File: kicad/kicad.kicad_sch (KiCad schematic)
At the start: 231 parts, among them sw1 Esc, sw10 Z, sw100 Num5, sw101 Num6, sw102 Num2, sw103 Num1, sw104 Num0, sw105 mPlay, sw106 mFwd, sw107 Num/, sw108 Num*, sw109 Num8, sw11 LCtrl, sw110 Num9, sw111 Num-, sw112 Num+, sw113 NumEnter, sw114 Num3, sw115 Num., sw12 LSys, sw13 F2, sw14 F3, sw15 2, sw16 3, sw17 W, sw18 E, sw19 S, sw2 F1, sw20 D, sw21 X, sw22 C, sw23 LAlt, sw24 THome, sw25 F4, sw26 F5, sw27 4, sw28 5, sw29 R, sw3 Tilda, sw30 T, sw31 F, sw32 G, sw33 V, sw34 B, sw35 LSpace, sw36 TLeft, sw37 F6, sw38 F7, sw39 6, sw4 1, sw40 7, sw41 Y, sw42 U, sw43 H, sw44 J, sw45 N, sw46 M, sw47 TUp, sw48 TDown, sw49 F8, sw5 Tab, sw50 F9, sw51 8, sw52 9, sw53 I, sw54 O, sw55 K, sw56 L, sw57 ,, sw58 ., sw59 RSpace, sw6 Q, sw60 TRight, sw61 F10, sw62 F11, sw63 0, sw64 -, sw65 P, sw66 [, sw67 ;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

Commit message: startup pcb
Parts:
- sw100: value Num5 -> N5
- sw101: value Num6 -> N6
- sw102: value Num2 -> N2
- sw103: value Num1 -> N1
- sw104: value Num0 -> N0
- sw105: value mPlay -> MPlay
- sw106: value mFwd -> MFwd
- sw107: value Num/ -> NSlash
- sw108: value Num* -> NStar
- sw109: value Num8 -> N8
- sw110: value Num9 -> N9
- sw111: value Num- -> NMinus
- sw112: value Num+ -> NPlus
- sw113: value NumEnter -> NEnter
- sw114: value Num3 -> N3
- sw115: value Num. -> NPeriod
- sw57: value , -> Comma
- sw58: value . -> Period
- sw64: value - -> Minus
- sw66: value [ -> LBrack
- sw67: value ; -> Semi
- sw68: value ' -> Quote
- sw69: value / -> FSlash
- sw75: value = -> Equals
- sw77: value ] -> RBrack
- sw78: value \ -> BSlash
- sw83: value ScrLck -> Scroll
- sw89: value Num4 -> N4
- sw94: value FN -> Fn
- sw95: value mBack -> MBack
- sw97: value NumLck -> NLock
- sw99: value Num7 -> N7

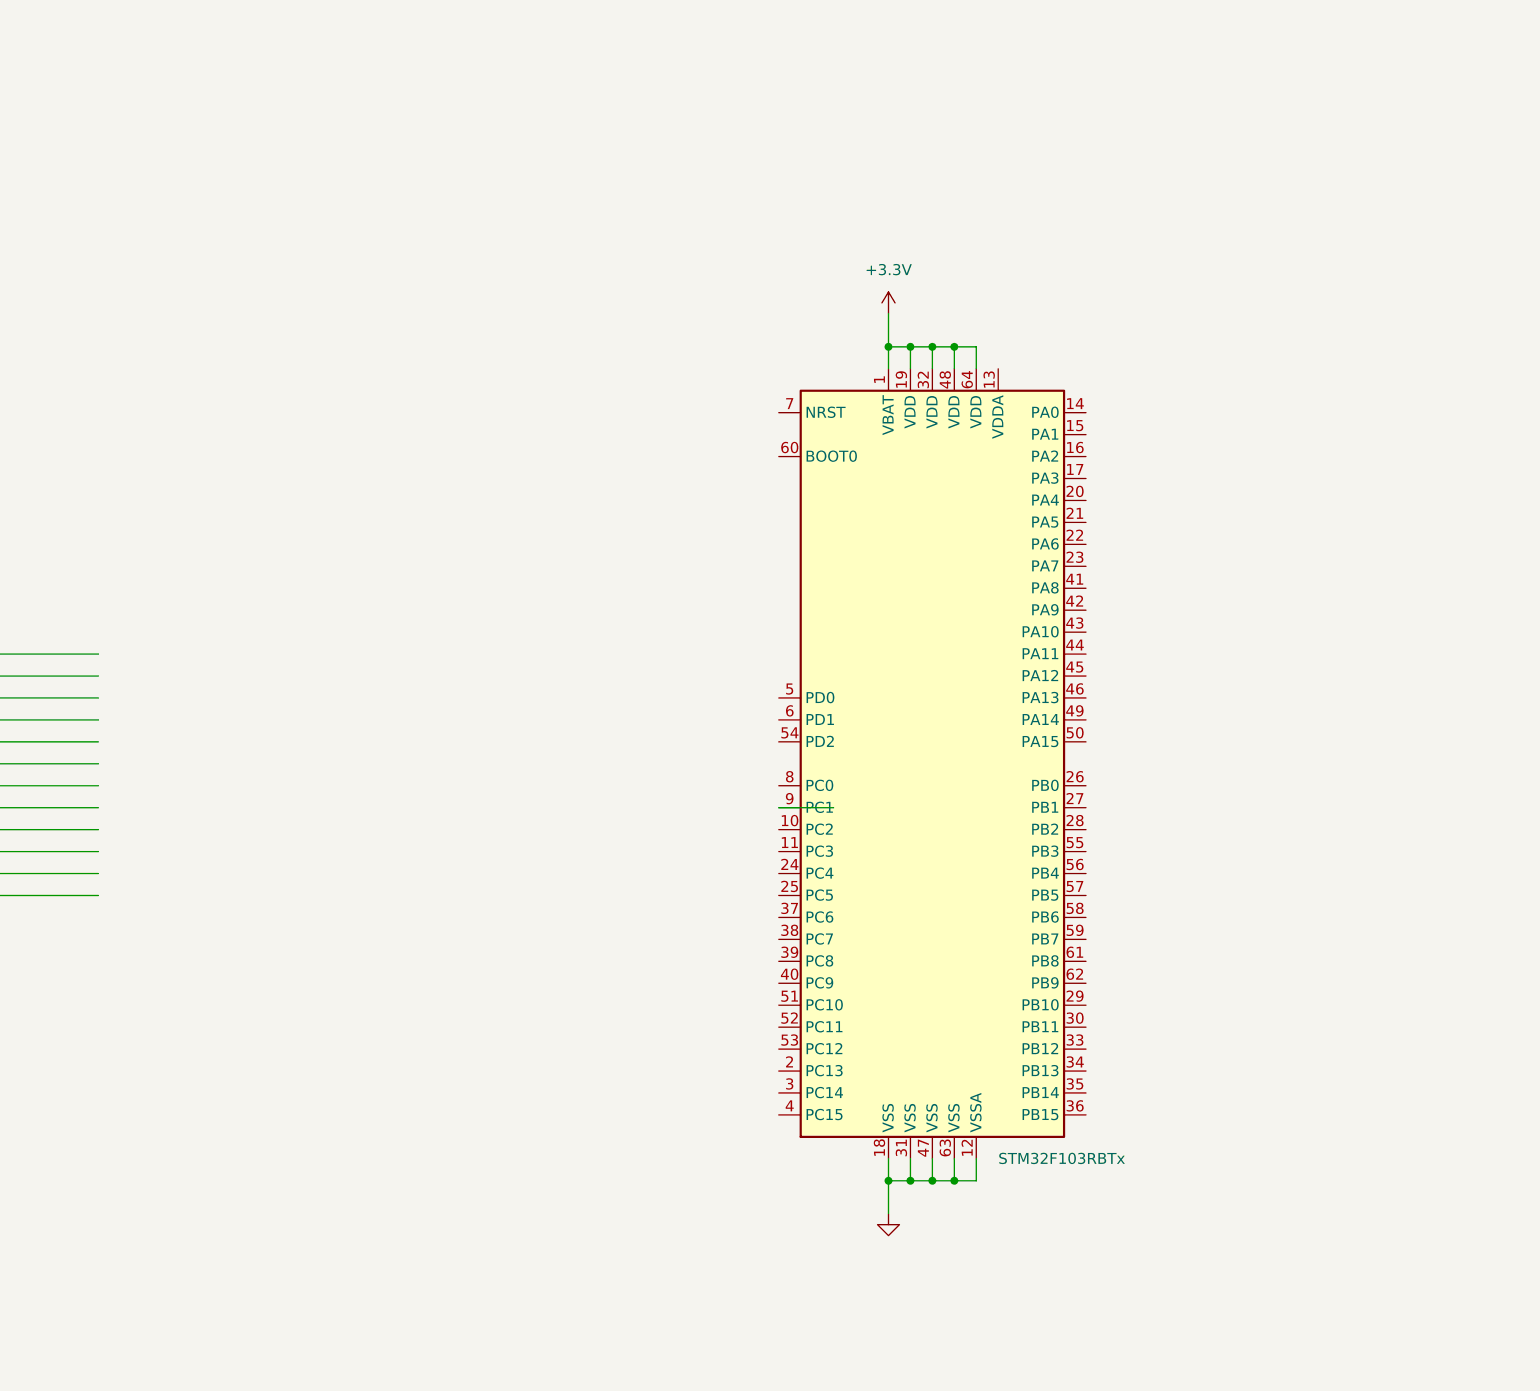
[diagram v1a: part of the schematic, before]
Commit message: Add decoupling circuits
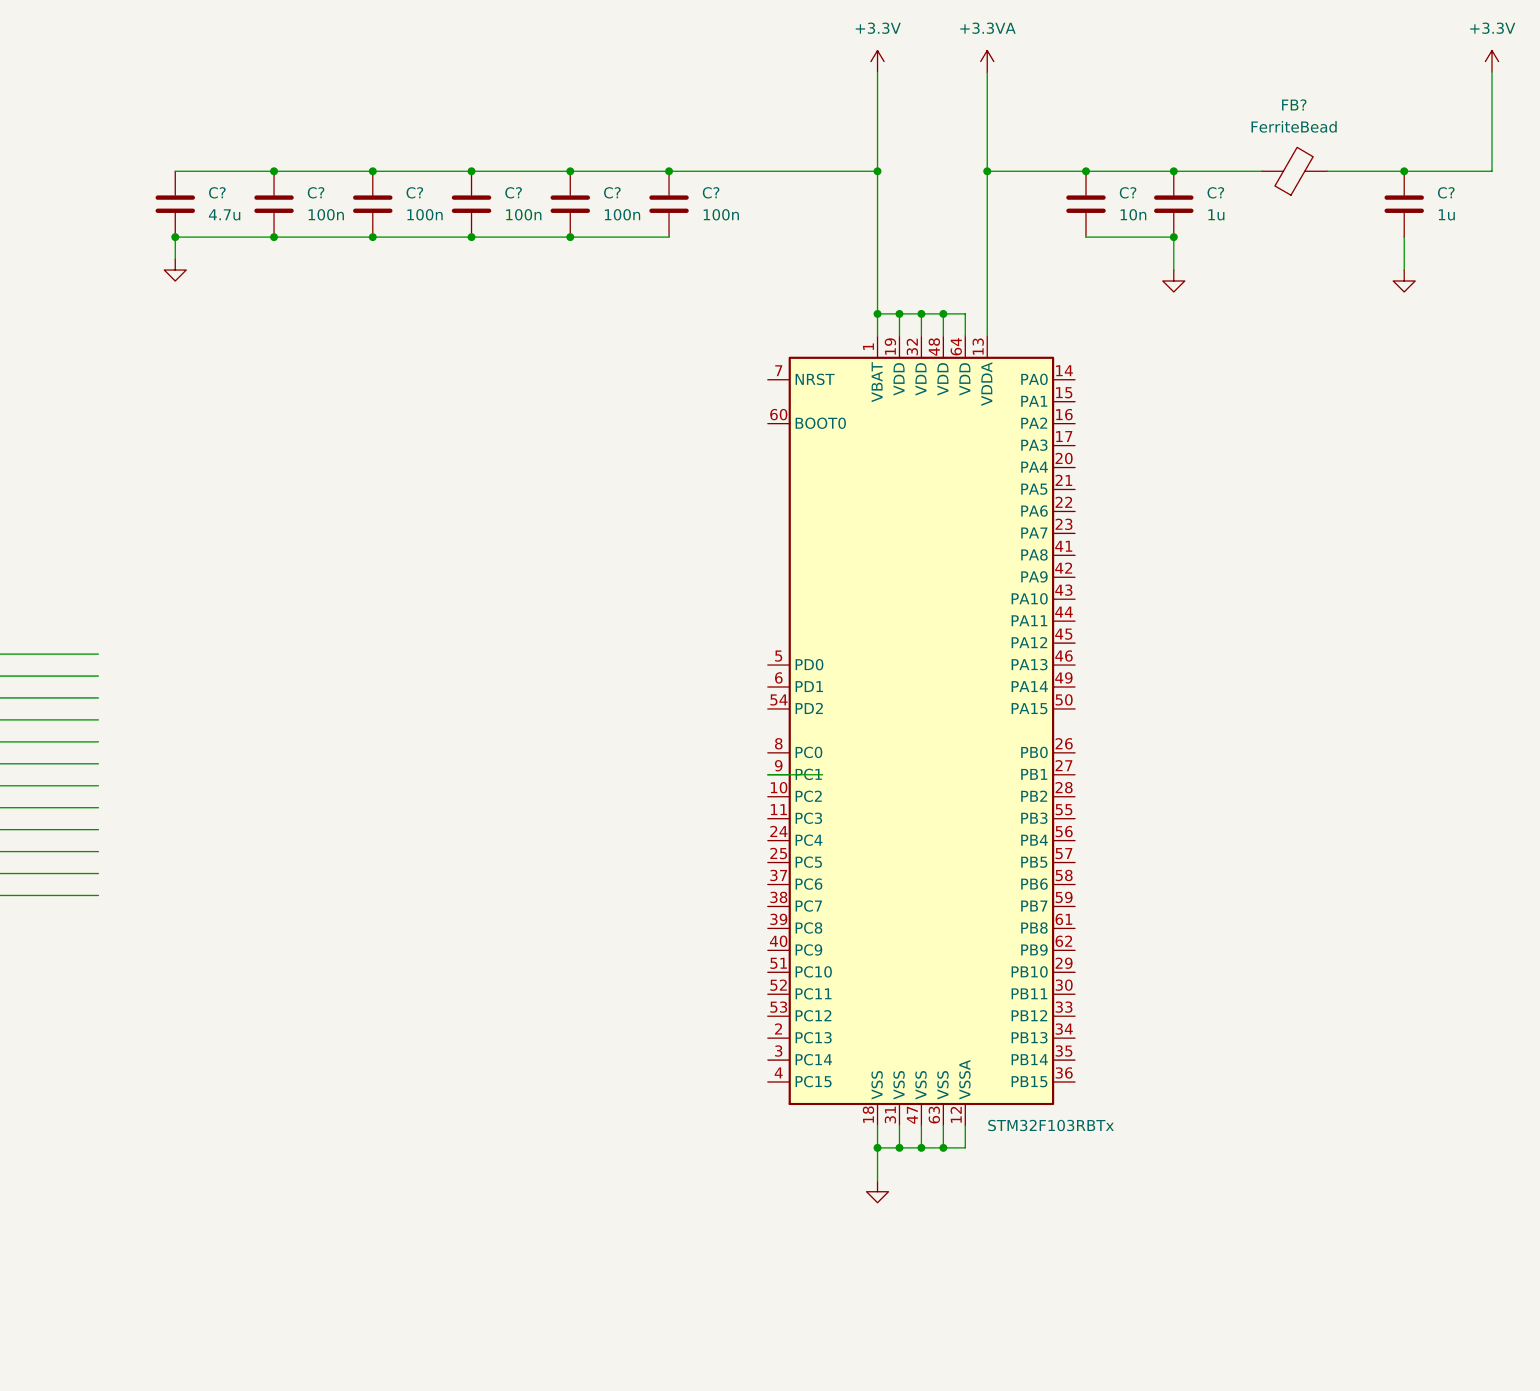
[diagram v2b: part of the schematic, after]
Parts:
- added C? (x5): 100n, symbol Device:C
- added C?: 10n, symbol Device:C
- added C? (x2): 1u, symbol Device:C
- added C?: 4.7u, symbol Device:C
- added FB?: FerriteBead, symbol Device:FerriteBead
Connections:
- net +3.3V: now also C?.1, C?.1, C?.1, C?.1, C?.1, C?.1, C?.1, FB?.2
- net GND: now also C?.2, C?.2, C?.2, C?.2, C?.2, C?.2, C?.2, C?.2, C?.2
- net +3.3VA: now reaches MCU1.13 (VDDA)
- net +3.3VA: now also C?.1, C?.1, FB?.1

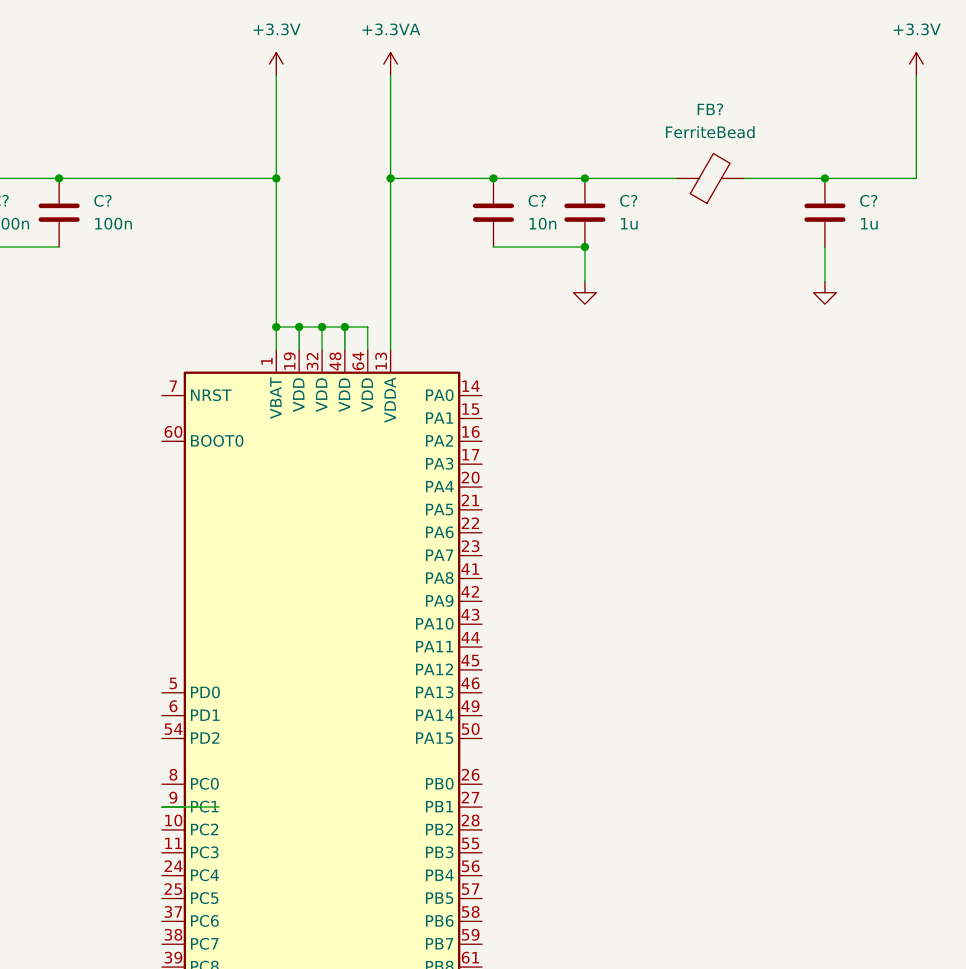
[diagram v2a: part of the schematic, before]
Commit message: fix decoupling for VDDA to just follow recommendations
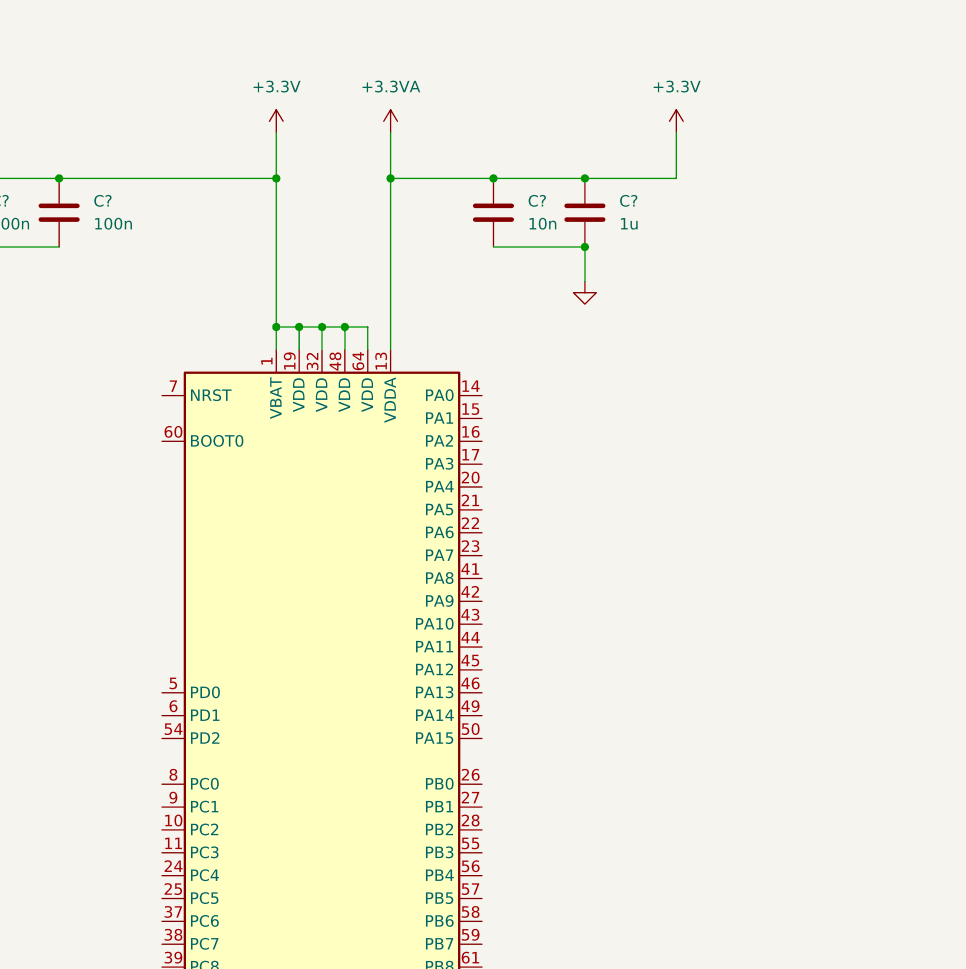
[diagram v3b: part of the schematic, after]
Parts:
- removed C?: 1u, symbol Device:C
- removed FB?: FerriteBead, symbol Device:FerriteBead
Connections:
- net +3.3VA is gone; now on net +3.3V: C?.1, C?.1, MCU1.13 (VDDA)
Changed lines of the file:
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@@
   (junction (at 149.86 105.41) (diameter 0) (color 0 0 0 0)
   )
-  (junction (at 368.3 40.64) (diameter 0) (color 0 0 0 0)
-  )
   (junction (at 74.93 33.02) (diameter 0) (color 0 0 0 0)
   )
@@
     (stroke (width 0) (type default) (color 0 0 0 0))
   )
-  (wire (pts (xy 368.3 48.26) (xy 368.3 52.07))
-    (stroke (width 0) (type default) (color 0 0 0 0))
-  )
   (wire (pts (xy 87.63 200.66) (xy 100.33 200.66))
     (stroke (width 0) (type default) (color 0 0 0 0))
@@
     (stroke (width 0) (type default) (color 0 0 0 0))
   )
-  (wire (pts (xy 294.64 110.49) (xy 300.99 110.49))
-    (stroke (width 0) (type default) (color 0 0 0 0))
-  )
   (wire (pts (xy 137.16 105.41) (xy 137.16 120.65))
     (stroke (width 0) (type default) (color 0 0 0 0))
@@
     (stroke (width 0) (type default) (color 0 0 0 0))
   )
-  (wire (pts (xy 368.3 40.64) (xy 378.46 40.64))
-    (stroke (width 0) (type default) (color 0 0 0 0))
-  )
   (wire (pts (xy 138.43 63.5) (xy 138.43 71.12))
     (stroke (width 0) (type default) (color 0 0 0 0))
@@
     (stroke (width 0) (type default) (color 0 0 0 0))
   )
-  (wire (pts (xy 320.04 29.21) (xy 320.04 40.64))
+  (wire (pts (xy 320.04 35.56) (xy 320.04 40.64))
     (stroke (width 0) (type default) (color 0 0 0 0))
   )
@@
     (stroke (width 0) (type default) (color 0 0 0 0))
   )
+  (wire (pts (xy 351.79 35.56) (xy 351.79 40.64))
+    (stroke (width 0) (type default) (color 0 0 0 0))
+  )
   (wire (pts (xy 151.13 120.65) (xy 149.86 120.65))
     (stroke (width 0) (type default) (color 0 0 0 0))
@@
     (stroke (width 0) (type default) (color 0 0 0 0))
   )
-  (wire (pts (xy 359.41 40.64) (xy 368.3 40.64))
-    (stroke (width 0) (type default) (color 0 0 0 0))
-  )
   (wire (pts (xy 135.89 208.28) (xy 135.89 212.09))
     (stroke (width 0) (type default) (color 0 0 0 0))
@@
     (stroke (width 0) (type default) (color 0 0 0 0))
   )
-  (wire (pts (xy 307.34 29.21) (xy 307.34 40.64))
+  (wire (pts (xy 307.34 35.56) (xy 307.34 40.64))
     (stroke (width 0) (type default) (color 0 0 0 0))
   )
@@
     (stroke (width 0) (type default) (color 0 0 0 0))
   )
-  (wire (pts (xy 378.46 29.21) (xy 378.46 40.64))
-    (stroke (width 0) (type default) (color 0 0 0 0))
-  )
   (wire (pts (xy 135.89 116.84) (xy 135.89 120.65))
     (stroke (width 0) (type default) (color 0 0 0 0))
@@
     (pin "2")
   )
-  (symbol (lib_id "Device:FerriteBead") (at 355.6 40.64 90) (unit 1)
-    (in_bom yes) (on_board yes) (fields_autoplaced)
-    (property "Reference" "FB?" (id 0) (at 355.5492 33.02 90))
-    (property "Value" "FerriteBead" (id 1) (at 355.5492 35.56 90))
-    (property "Footprint" "" (id 2) (at 355.6 42.418 90)
-      (effects (font (size 1.27 1.27)) hide)
-    )
-    (property "Datasheet" "~" (id 3) (at 355.6 40.64 0)
-      (effects (font (size 1.27 1.27)) hide)
-    )
-    (pin "1")
-    (pin "2")
-  )
   (symbol (lib_id "pspice:DIODE") (at 130.81 74.93 180) (unit 1)
     (in_bom yes) (on_board yes) (fields_autoplaced)
@@
     (pin "2")
   )
-  (symbol (lib_id "power:+3.3V") (at 307.34 29.21 0) (unit 1)
+  (symbol (lib_id "power:+3.3V") (at 307.34 35.56 0) (unit 1)
     (in_bom yes) (on_board yes) (fields_autoplaced)
-    (property "Reference" "#PWR0102" (id 0) (at 307.34 33.02 0)
+    (property "Reference" "#PWR0102" (id 0) (at 307.34 39.37 0)
       (effects (font (size 1.27 1.27)) hide)
     )
-    (property "Value" "+3.3V" (id 1) (at 307.34 24.13 0))
-    (property "Footprint" "" (id 2) (at 307.34 29.21 0)
+    (property "Value" "+3.3V" (id 1) (at 307.34 30.48 0))
+    (property "Footprint" "" (id 2) (at 307.34 35.56 0)
       (effects (font (size 1.27 1.27)) hide)
     )
-    (property "Datasheet" "" (id 3) (at 307.34 29.21 0)
+    (property "Datasheet" "" (id 3) (at 307.34 35.56 0)
       (effects (font (size 1.27 1.27)) hide)
     )
@@
     (pin "2")
   )
-  (symbol (lib_id "power:+3.3VA") (at 320.04 29.21 0) (unit 1)
+  (symbol (lib_id "power:+3.3VA") (at 320.04 35.56 0) (unit 1)
     (in_bom yes) (on_board yes) (fields_autoplaced)
-    (property "Reference" "#PWR?" (id 0) (at 320.04 33.02 0)
+    (property "Reference" "#PWR?" (id 0) (at 320.04 39.37 0)
       (effects (font (size 1.27 1.27)) hide)
     )
-    (property "Value" "+3.3VA" (id 1) (at 320.04 24.13 0))
-    (property "Footprint" "" (id 2) (at 320.04 29.21 0)
+    (property "Value" "+3.3VA" (id 1) (at 320.04 30.48 0))
+    (property "Footprint" "" (id 2) (at 320.04 35.56 0)
       (effects (font (size 1.27 1.27)) hide)
     )
-    (property "Datasheet" "" (id 3) (at 320.04 29.21 0)
+    (property "Datasheet" "" (id 3) (at 320.04 35.56 0)
       (effects (font (size 1.27 1.27)) hide)
     )
@@
     (pin "2")
   )
-  (symbol (lib_id "power:+3.3V") (at 378.46 29.21 0) (unit 1)
+  (symbol (lib_id "power:+3.3V") (at 351.79 35.56 0) (unit 1)
     (in_bom yes) (on_board yes) (fields_autoplaced)
-    (property "Reference" "#PWR?" (id 0) (at 378.46 33.02 0)
+    (property "Reference" "#PWR?" (id 0) (at 351.79 39.37 0)
       (effects (font (size 1.27 1.27)) hide)
     )
-    (property "Value" "+3.3V" (id 1) (at 378.46 24.13 0))
-    (property "Footprint" "" (id 2) (at 378.46 29.21 0)
+    (property "Value" "+3.3V" (id 1) (at 351.79 30.48 0))
+    (property "Footprint" "" (id 2) (at 351.79 35.56 0)
       (effects (font (size 1.27 1.27)) hide)
     )
-    (property "Datasheet" "" (id 3) (at 378.46 29.21 0)
+    (property "Datasheet" "" (id 3) (at 351.79 35.56 0)
       (effects (font (size 1.27 1.27)) hide)
     )
@@
     (pin "2")
   )
-  (symbol (lib_id "power:GND") (at 368.3 52.07 0) (unit 1)
-    (in_bom yes) (on_board yes) (fields_autoplaced)
-    (property "Reference" "#PWR?" (id 0) (at 368.3 58.42 0)
-      (effects (font (size 1.27 1.27)) hide)
-    )
-    (property "Value" "GND" (id 1) (at 368.3 57.15 0)
-      (effects (font (size 1.27 1.27)) hide)
-    )
-    (property "Footprint" "" (id 2) (at 368.3 52.07 0)
-      (effects (font (size 1.27 1.27)) hide)
-    )
-    (property "Datasheet" "" (id 3) (at 368.3 52.07 0)
-      (effects (font (size 1.27 1.27)) hide)
-    )
-    (pin "1")
-  )
   (symbol (lib_id "pspice:DIODE") (at 80.01 181.61 180) (unit 1)
     (in_bom yes) (on_board yes) (fields_autoplaced)
@@
     (pin "2")
   )
-  (symbol (lib_id "Device:C") (at 368.3 44.45 0) (unit 1)
-    (in_bom yes) (on_board yes) (fields_autoplaced)
-    (property "Reference" "C?" (id 0) (at 372.11 43.1799 0)
-      (effects (font (size 1.27 1.27)) (justify left))
-    )
-    (property "Value" "1u" (id 1) (at 372.11 45.7199 0)
-      (effects (font (size 1.27 1.27)) (justify left))
-    )
-    (property "Footprint" "" (id 2) (at 369.2652 48.26 0)
-      (effects (font (size 1.27 1.27)) hide)
-    )
-    (property "Datasheet" "~" (id 3) (at 368.3 44.45 0)
-      (effects (font (size 1.27 1.27)) hide)
-    )
-    (pin "1")
-    (pin "2")
-  )
   (symbol (lib_id "pspice:DIODE") (at 80.01 196.85 180) (unit 1)
     (in_bom yes) (on_board yes) (fields_autoplaced)
@@
       (reference "#PWR?") (unit 1) (value "GND") (footprint "")
     )
-    (path "/bc8ac47c-1c77-4427-b255-ccb07c869ad8"
-      (reference "#PWR?") (unit 1) (value "GND") (footprint "")
-    )
     (path "/c469a32f-d4ac-4add-a99b-6ec47ca9501b"
       (reference "#PWR?") (unit 1) (value "GND") (footprint "")
@@
       (reference "C?") (unit 1) (value "100n") (footprint "")
     )
-    (path "/f8d89918-453e-420c-8dd7-ebdc360f7e55"
-      (reference "C?") (unit 1) (value "1u") (footprint "")
-    )
     (path "/05652d3e-64eb-4703-bf61-023ecd3c8890"
       (reference "D1") (unit 1) (value "D-Esc") (footprint "Diode_SMD:D_SOD-123F")
@@
       (reference "D115") (unit 1) (value "D-Num.") (footprint "Diode_SMD:D_SOD-123F")
     )
-    (path "/39b89246-14c1-4274-ad90-5f58b034c7f7"
-      (reference "FB?") (unit 1) (value "FerriteBead") (footprint "")
-    )
     (path "/f1a6840b-d519-4bc8-adf0-9bed5052e1c8"
